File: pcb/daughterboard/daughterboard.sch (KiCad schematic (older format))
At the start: 7 parts, among them J1 Conn_01x04

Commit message: redid daughterboard
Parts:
- added H1, H2, H3: MountingHole_Pad, keebs:m2.5_pad_via, symbol Mechanical:MountingHole_Pad
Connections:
- net GND: now also H1.1, H2.1, H3.1
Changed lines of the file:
@@
-	1    0    0    -1
-$EndComp
-$Comp
-L power:GND #PWR0108
-U 1 1 5CC13C84
-P 3750 5050
-F 0 "#PWR0108" H 3750 4800 50  0001 C CNN
-F 1 "GND" V 3755 4922 50  0000 R CNN
-F 2 "" H 3750 5050 50  0001 C CNN
-F 3 "" H 3750 5050 50  0001 C CNN
-	1    3750 5050
 	1    0    0    -1
 $EndComp
@@
 Text Label 4850 2600 0    50   ~ 0
 d-
+$Comp
+L Mechanical:MountingHole_Pad H1
+U 1 1 5CE8E580
+P 6400 3250
+F 0 "H1" H 6500 3299 50  0000 L CNN
+F 1 "MountingHole_Pad" H 6500 3208 50  0000 L CNN
+F 2 "keebs:m2.5_pad_via" H 6400 3250 50  0001 C CNN
+F 3 "~" H 6400 3250 50  0001 C CNN
+	1    6400 3250
+	1    0    0    -1
+$EndComp
+$Comp
+L power:GND #PWR02
+U 1 1 5CE8EEC8
+P 6400 3350
+F 0 "#PWR02" H 6400 3100 50  0001 C CNN
+F 1 "GND" V 6405 3222 50  0000 R CNN
+F 2 "" H 6400 3350 50  0001 C CNN
+F 3 "" H 6400 3350 50  0001 C CNN
+	1    6400 3350
+	1    0    0    -1
+$EndComp
+$Comp
+L Mechanical:MountingHole_Pad H2
+U 1 1 5CE90C0E
+P 6400 3800
+F 0 "H2" H 6500 3849 50  0000 L CNN
+F 1 "MountingHole_Pad" H 6500 3758 50  0000 L CNN
+F 2 "keebs:m2.5_pad_via" H 6400 3800 50  0001 C CNN
+F 3 "~" H 6400 3800 50  0001 C CNN
+	1    6400 3800
+	1    0    0    -1
+$EndComp
+$Comp
+L power:GND #PWR03
+U 1 1 5CE90C14
+P 6400 3900
+F 0 "#PWR03" H 6400 3650 50  0001 C CNN
+F 1 "GND" V 6405 3772 50  0000 R CNN
+F 2 "" H 6400 3900 50  0001 C CNN
+F 3 "" H 6400 3900 50  0001 C CNN
+	1    6400 3900
+	1    0    0    -1
+$EndComp
+$Comp
+L Mechanical:MountingHole_Pad H3
+U 1 1 5CE917F5
+P 6400 4350
+F 0 "H3" H 6500 4399 50  0000 L CNN
+F 1 "MountingHole_Pad" H 6500 4308 50  0000 L CNN
+F 2 "keebs:m2.5_pad_via" H 6400 4350 50  0001 C CNN
+F 3 "~" H 6400 4350 50  0001 C CNN
+	1    6400 4350
+	1    0    0    -1
+$EndComp
+$Comp
+L power:GND #PWR04
+U 1 1 5CE917FB
+P 6400 4450
+F 0 "#PWR04" H 6400 4200 50  0001 C CNN
+F 1 "GND" V 6405 4322 50  0000 R CNN
+F 2 "" H 6400 4450 50  0001 C CNN
+F 3 "" H 6400 4450 50  0001 C CNN
+	1    6400 4450
+	1    0    0    -1
+$EndComp
 $EndSCHEMATC

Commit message: daughterboard updates
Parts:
- J1: footprint Connector_JST:JST_SH_SM04B-SRSS-TB_1x04-1MP_P1.00mm_Horizontal -> Connector_PinHeader_2.00mm:PinHeader_1x04_P2.00mm_Vertical
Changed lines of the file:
@@
 F 0 "J1" H 5120 3125 50  0000 C CNN
 F 1 "Conn_01x04" H 5120 3216 50  0000 C CNN
-F 2 "Connector_JST:JST_SH_SM04B-SRSS-TB_1x04-1MP_P1.00mm_Horizontal" H 5200 3550 50  0001 C CNN
+F 2 "Connector_PinHeader_2.00mm:PinHeader_1x04_P2.00mm_Vertical" H 5200 3550 50  0001 C CNN
 F 3 "~" H 5200 3550 50  0001 C CNN
 	1    5200 3550

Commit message: smol updates
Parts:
- F1: value PTC -> 500mA
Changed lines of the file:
@@
 	0    1    1    0
-$EndComp
-$Comp
-L keyboard_parts:PTC F1
-U 1 1 5CBDEF9D
-P 4450 4500
-F 0 "F1" H 4450 4815 50  0000 C CNN
-F 1 "PTC" H 4450 4724 50  0000 C CNN
-F 2 "Fuse:Fuse_0805_2012Metric" V 4450 4500 60  0001 C CNN
-F 3 "" V 4450 4500 60  0000 C CNN
-	1    4450 4500
-	1    0    0    -1
 $EndComp
 Wire Wire Line
@@
 	1    0    0    -1
 $EndComp
+$Comp
+L keyboard_parts:PTC F1
+U 1 1 5CBDEF9D
+P 4450 4500
+F 0 "F1" H 4450 4815 50  0000 C CNN
+F 1 "500mA" H 4450 4724 50  0000 C CNN
+F 2 "Fuse:Fuse_0805_2012Metric" V 4450 4500 60  0001 C CNN
+F 3 "" V 4450 4500 60  0000 C CNN
+	1    4450 4500
+	1    0    0    -1
+$EndComp

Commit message: prepared for pcba
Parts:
- added J2: Conn_01x04, Connector_JST:JST_SH_SM04B-SRSS-TB_1x04-1MP_P1.00mm_Horizontal, symbol Connector_Generic:Conn_01x04
- F1: symbol keyboard_parts:PTC -> daughterboard-rescue:PTC-keyboard_parts
- R1, R2: symbol keyboard_parts:R -> daughterboard-rescue:R-keyboard_parts
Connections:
- net GND: now also J2.1 (Pin_1)
- net VCC: now also J2.4 (Pin_4)
- net d+: now also J2.2 (Pin_2)
- net d-: now also J2.3 (Pin_3)
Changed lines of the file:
@@
 EESchema Schematic File Version 4
 LIBS:daughterboard-cache
-EELAYER 29 0
+EELAYER 30 0
 EELAYER END
 $Descr A4 11693 8268
@@
 $EndComp
 $Comp
-L keyboard_parts:R R1
+L daughterboard-rescue:R-keyboard_parts R1
 U 1 1 5C9F39A7
 P 2950 3350
@@
 NoConn ~ 2700 3850
 $Comp
-L keyboard_parts:R R2
+L daughterboard-rescue:R-keyboard_parts R2
 U 1 1 5C9F3F4F
 P 2950 3950
@@
 $EndComp
 $Comp
-L keyboard_parts:PTC F1
+L daughterboard-rescue:PTC-keyboard_parts F1
 U 1 1 5CBDEF9D
 P 4450 4500
@@
 	1    0    0    -1
 $EndComp
+$Comp
+L Connector_Generic:Conn_01x04 J2
+U 1 1 5DF47513
+P 5550 3550
+F 0 "J2" H 5470 3125 50  0000 C CNN
+F 1 "Conn_01x04" H 5470 3216 50  0000 C CNN
+F 2 "Connector_JST:JST_SH_SM04B-SRSS-TB_1x04-1MP_P1.00mm_Horizontal" H 5550 3550 50  0001 C CNN
+F 3 "~" H 5550 3550 50  0001 C CNN
+	1    5550 3550
+	1    0    0    -1
+$EndComp
+Wire Wire Line
+	5000 3650 5350 3650
+Connection ~ 5000 3650
+Wire Wire Line
+	5000 3550 5350 3550
+Connection ~ 5000 3550
+Wire Wire Line
+	5000 3450 5350 3450
+Connection ~ 5000 3450
+Wire Wire Line
+	5000 3750 5350 3750
+Connection ~ 5000 3750
 $EndSCHEMATC

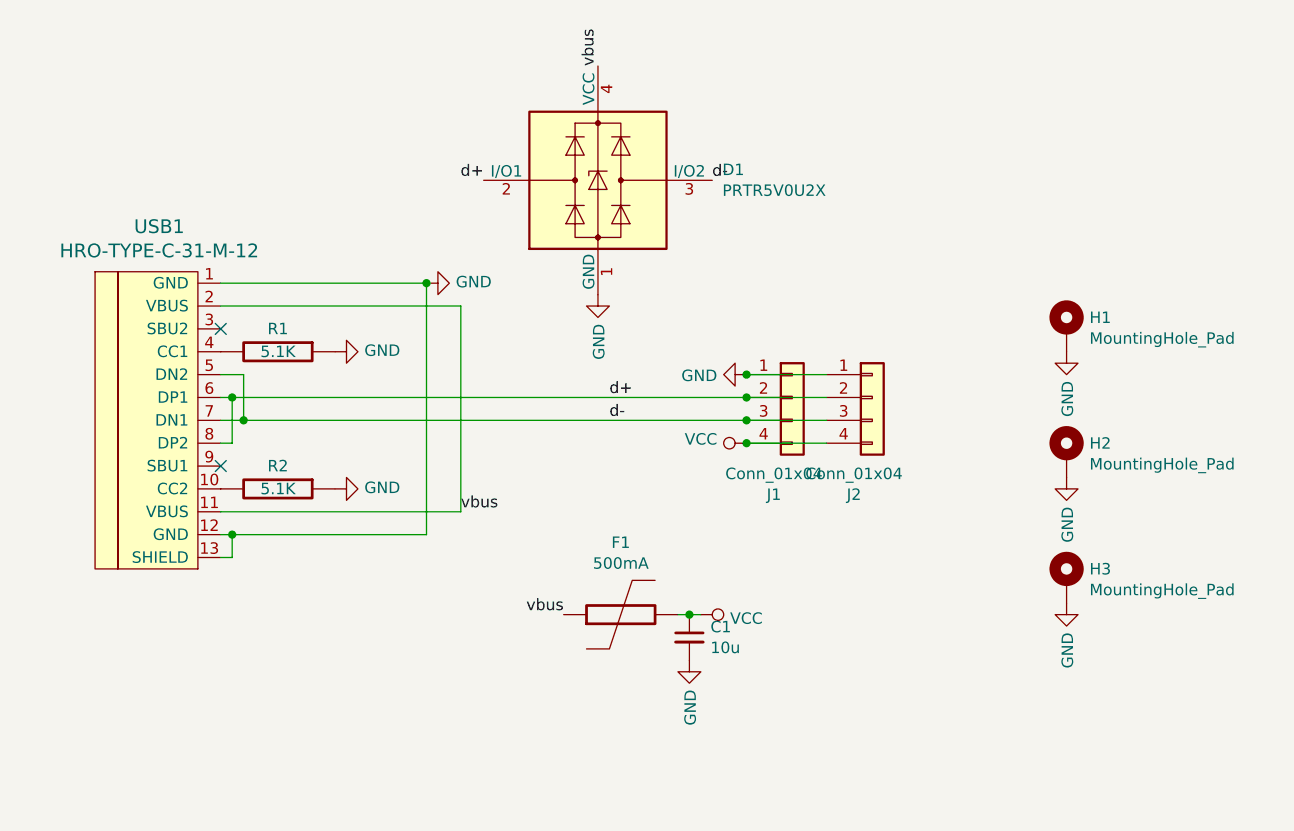
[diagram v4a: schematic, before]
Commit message: edited LED circuit, flipped stabs
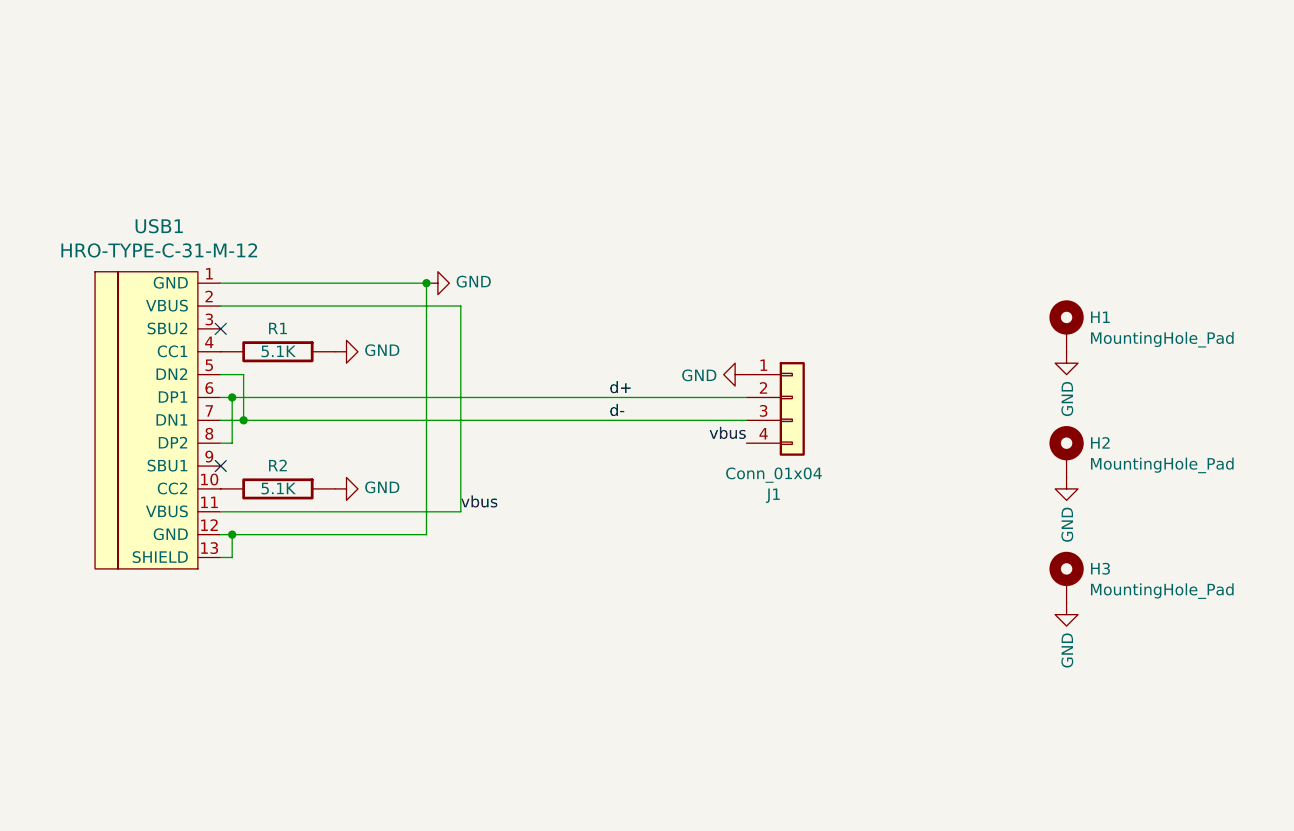
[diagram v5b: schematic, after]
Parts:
- removed C1: 10u, Capacitor_SMD:C_0603_1608Metric, symbol Device:C_Small
- removed D1: PRTR5V0U2X, Package_TO_SOT_SMD:SOT-143, symbol Power_Protection:PRTR5V0U2X
- removed F1: 500mA, Fuse:Fuse_0805_2012Metric, symbol daughterboard-rescue:PTC-keyboard_parts
- removed J2: Conn_01x04, Connector_JST:JST_SH_SM04B-SRSS-TB_1x04-1MP_P1.00mm_Horizontal, symbol Connector_Generic:Conn_01x04
- J1: footprint Connector_PinHeader_2.00mm:PinHeader_1x04_P2.00mm_Vertical -> Connector_JST:JST_SH_SM04B-SRSS-TB_1x04-1MP_P1.00mm_Horizontal
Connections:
- net VCC is gone; now on net vbus: J1.4 (Pin_4)
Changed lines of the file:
@@
 Wire Wire Line
 	3750 3150 2700 3150
-$Comp
-L Device:C_Small C1
-U 1 1 5CBDEE30
-P 4750 4600
-F 0 "C1" H 4842 4646 50  0000 L CNN
-F 1 "10u" H 4842 4555 50  0000 L CNN
-F 2 "Capacitor_SMD:C_0603_1608Metric" H 4750 4600 50  0001 C CNN
-F 3 "~" H 4750 4600 50  0001 C CNN
-	1    4750 4600
-	1    0    0    -1
-$EndComp
-$Comp
-L power:VCC #PWR0106
-U 1 1 5C9F40F7
-P 4800 4500
-F 0 "#PWR0106" H 4800 4350 50  0001 C CNN
-F 1 "VCC" V 4817 4628 50  0000 L CNN
-F 2 "" H 4800 4500 50  0001 C CNN
-F 3 "" H 4800 4500 50  0001 C CNN
-	1    4800 4500
-	0    1    1    0
-$EndComp
-Wire Wire Line
-	4700 4500 4750 4500
-Connection ~ 4750 4500
-Wire Wire Line
-	4750 4500 4800 4500
-$Comp
-L power:GND #PWR0107
-U 1 1 5CBDF319
-P 4750 4700
-F 0 "#PWR0107" H 4750 4450 50  0001 C CNN
-F 1 "GND" V 4755 4572 50  0000 R CNN
-F 2 "" H 4750 4700 50  0001 C CNN
-F 3 "" H 4750 4700 50  0001 C CNN
-	1    4750 4700
-	1    0    0    -1
-$EndComp
 Text Label 4400 3650 0    50   ~ 0
 d-
@@
 $EndComp
 $Comp
-L power:VCC #PWR0102
-U 1 1 5C9F36A7
-P 5000 3750
-F 0 "#PWR0102" H 5000 3600 50  0001 C CNN
-F 1 "VCC" V 5017 3878 50  0000 L CNN
-F 2 "" H 5000 3750 50  0001 C CNN
-F 3 "" H 5000 3750 50  0001 C CNN
-	1    5000 3750
-	0    -1   -1   0
-$EndComp
-$Comp
 L Connector_Generic:Conn_01x04 J1
 U 1 1 5C9F357E
@@
 F 0 "J1" H 5120 3125 50  0000 C CNN
 F 1 "Conn_01x04" H 5120 3216 50  0000 C CNN
-F 2 "Connector_PinHeader_2.00mm:PinHeader_1x04_P2.00mm_Vertical" H 5200 3550 50  0001 C CNN
+F 2 "Connector_JST:JST_SH_SM04B-SRSS-TB_1x04-1MP_P1.00mm_Horizontal" H 5200 3550 50  0001 C CNN
 F 3 "~" H 5200 3550 50  0001 C CNN
 	1    5200 3550
@@
 	5000 3650 2800 3650
 Connection ~ 2800 3650
-$Comp
-L Power_Protection:PRTR5V0U2X D1
-U 1 1 5CC057A0
-P 4350 2600
-F 0 "D1" H 4894 2646 50  0000 L CNN
-F 1 "PRTR5V0U2X" H 4894 2555 50  0000 L CNN
-F 2 "Package_TO_SOT_SMD:SOT-143" H 4410 2600 50  0001 C CNN
-F 3 "https://assets.nexperia.com/documents/data-sheet/PRTR5V0U2X.pdf" H 4410 2600 50  0001 C CNN
-	1    4350 2600
-	1    0    0    -1
-$EndComp
-$Comp
-L power:GND #PWR01
-U 1 1 5CC06479
-P 4350 3100
-F 0 "#PWR01" H 4350 2850 50  0001 C CNN
-F 1 "GND" V 4355 2972 50  0000 R CNN
-F 2 "" H 4350 3100 50  0001 C CNN
-F 3 "" H 4350 3100 50  0001 C CNN
-	1    4350 3100
-	1    0    0    -1
-$EndComp
 Text Label 3750 4050 0    50   ~ 0
 vbus
-Text Label 4200 4500 2    50   ~ 0
-vbus
-Text Label 4350 2100 1    50   ~ 0
-vbus
-Text Label 3850 2600 2    50   ~ 0
-d+
-Text Label 4850 2600 0    50   ~ 0
-d-
 $Comp
 L Mechanical:MountingHole_Pad H1
@@
 	1    0    0    -1
 $EndComp
-$Comp
-L daughterboard-rescue:PTC-keyboard_parts F1
-U 1 1 5CBDEF9D
-P 4450 4500
-F 0 "F1" H 4450 4815 50  0000 C CNN
-F 1 "500mA" H 4450 4724 50  0000 C CNN
-F 2 "Fuse:Fuse_0805_2012Metric" V 4450 4500 60  0001 C CNN
-F 3 "" V 4450 4500 60  0000 C CNN
-	1    4450 4500
-	1    0    0    -1
-$EndComp
-$Comp
-L Connector_Generic:Conn_01x04 J2
-U 1 1 5DF47513
-P 5550 3550
-F 0 "J2" H 5470 3125 50  0000 C CNN
-F 1 "Conn_01x04" H 5470 3216 50  0000 C CNN
-F 2 "Connector_JST:JST_SH_SM04B-SRSS-TB_1x04-1MP_P1.00mm_Horizontal" H 5550 3550 50  0001 C CNN
-F 3 "~" H 5550 3550 50  0001 C CNN
-	1    5550 3550
-	1    0    0    -1
-$EndComp
-Wire Wire Line
-	5000 3650 5350 3650
-Connection ~ 5000 3650
-Wire Wire Line
-	5000 3550 5350 3550
-Connection ~ 5000 3550
-Wire Wire Line
-	5000 3450 5350 3450
-Connection ~ 5000 3450
-Wire Wire Line
-	5000 3750 5350 3750
-Connection ~ 5000 3750
+Text Label 5000 3750 2    50   ~ 0
+vbus
 $EndSCHEMATC
